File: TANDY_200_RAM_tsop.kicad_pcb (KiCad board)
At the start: 2 copper layers, 35.6 x 20.3 mm, 4 parts, among them J1 TANDY_26-3688, U1 62256, U2 74LVC2G00

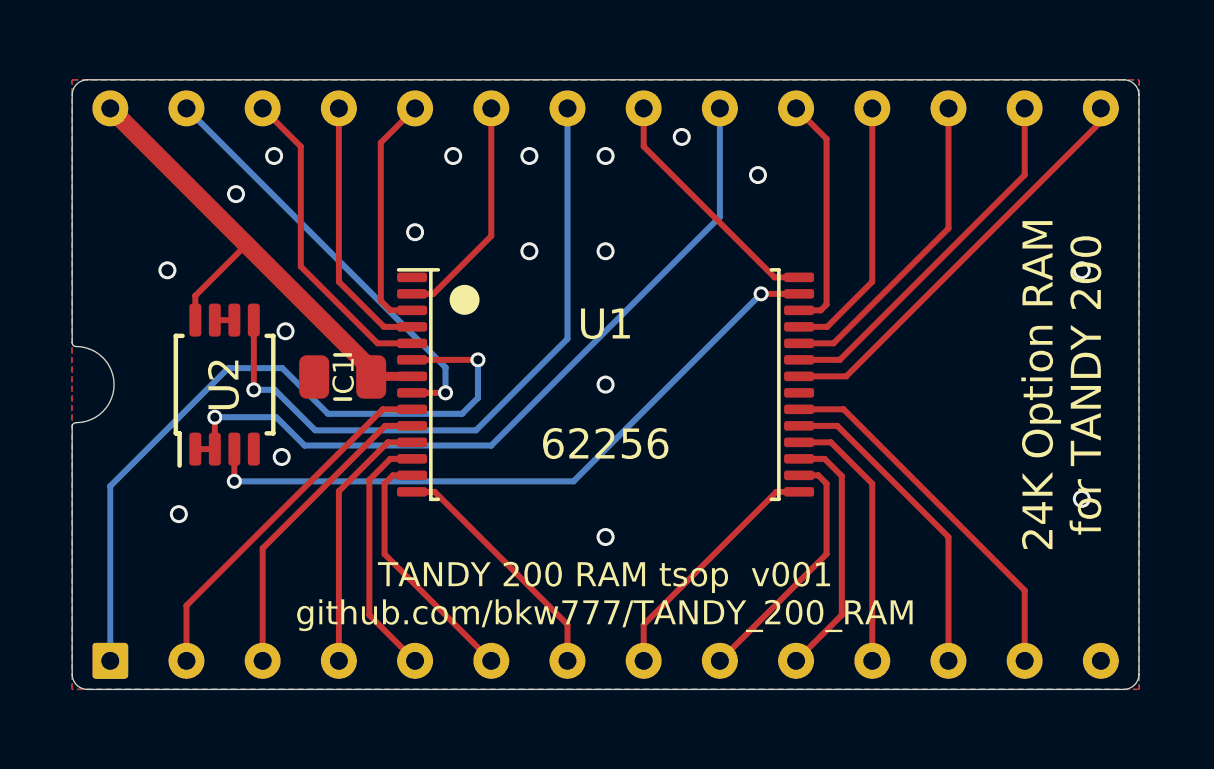
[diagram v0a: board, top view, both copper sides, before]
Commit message: ground paths, footprints, sch symbols
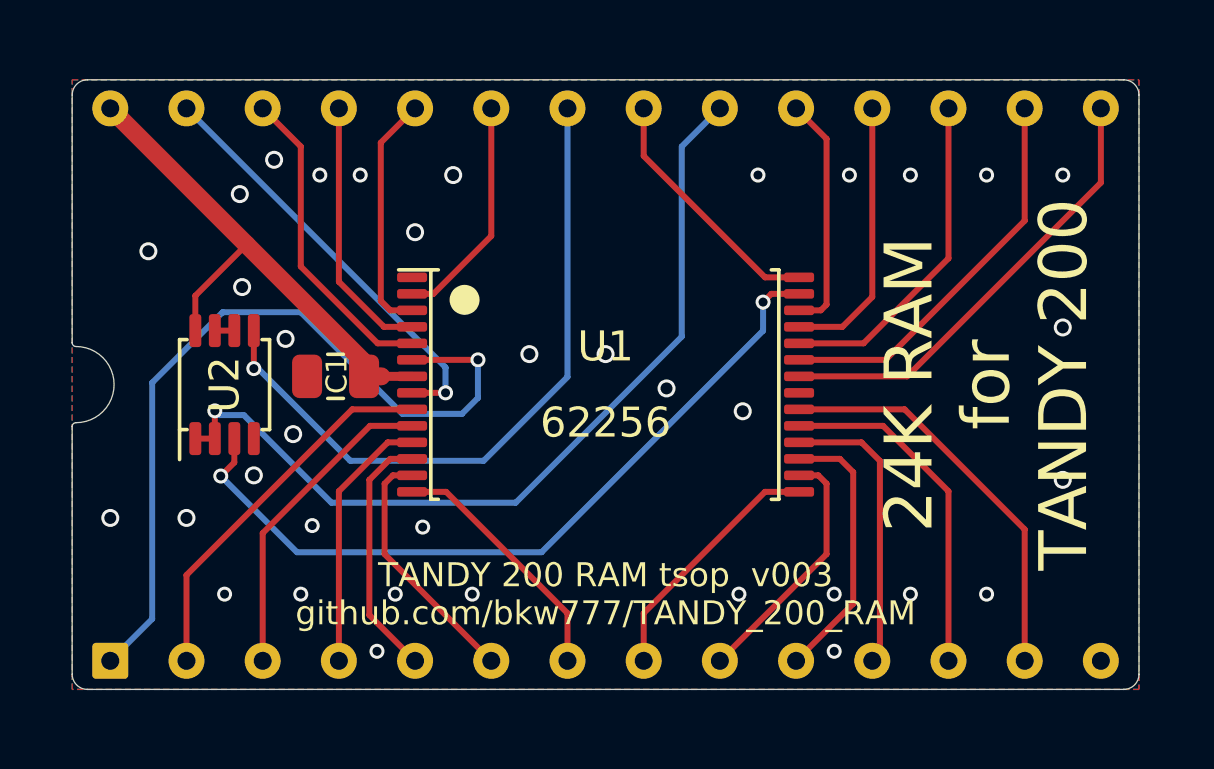
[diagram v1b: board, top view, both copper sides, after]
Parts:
- U1: footprint 000_LOCAL:TSOP-28-alt -> 000_LOCAL:TSOP-28
- U2: footprint 000_LOCAL:SOT-505-2 -> 000_LOCAL:SSOP-8_2.95x2.8x0.65
- moved C1 0.24 mm to (130.6, 105.6)
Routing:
- net /~{CE}: track 22.5 -> 25.9 mm
- net /~{CS1}: track 25.7 -> 28.8 mm
- net /~{WE}: track 24.0 -> 26.8 mm
- net /D2: track 12.4 -> 13.6 mm
- net /D3: track 14.0 -> 15.2 mm
- net /D1: track 10.6 -> 11.5 mm
- net /D4: track 12.3 -> 13.2 mm
- net /CS2: track 22.3 -> 23.1 mm
- net /D0: track 8.92 -> 9.72 mm
- net /A0: track 8.45 -> 9.07 mm
- net /A12: track 12.1 -> 12.7 mm
- net /D5: track 10.6 -> 11.2 mm
- net GND: vias 18 -> 36
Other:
- board text added: "24K RAM for TANDY 200"
- board text removed: "24K Option RAM for TANDY 200"

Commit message: 24k tsop layout and all board outlines expanded slightly
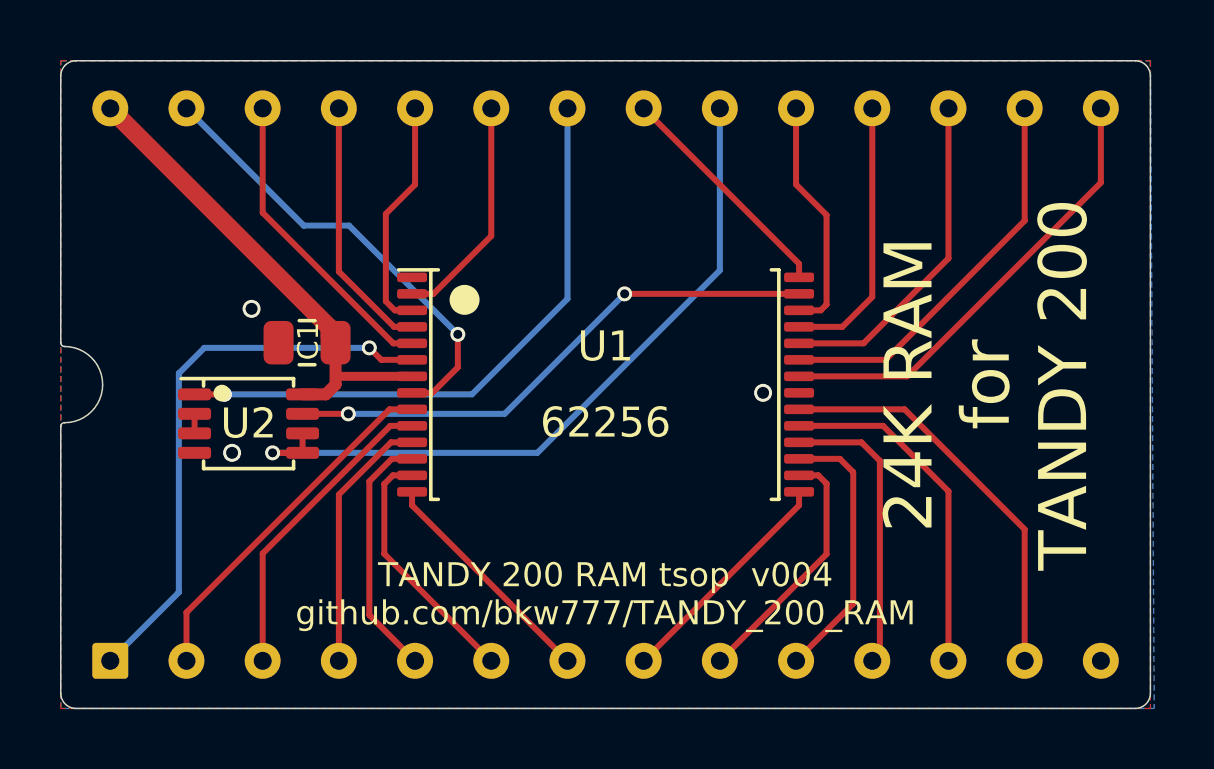
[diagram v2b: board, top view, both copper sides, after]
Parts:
- J1: footprint 000_LOCAL:KEL ICC05-028-360TP PCB -> 000_LOCAL:KEL ICC05-028-360TP
- moved U2 1.53 mm to (127.7, 107.2), turned to 0 degrees
- moved C1 1.47 mm to (129.6, 104.5)
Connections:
- U2 pad 1: /~{CS1} -> /CS2
- U2 pad 2: /~{CS1} -> Net-(U2-Pad2)
- U2 pad 3: /~{CE} -> Net-(U2-Pad2)
- U2 pad 5: /CS2 -> /~{CS1}
- U2 pad 6: Net-(U2-Pad6) -> /~{CS1}
- U2 pad 7: Net-(U2-Pad6) -> /~{CE}
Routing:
- net /~{WE}: track 26.8 -> 18.8 mm
- net /~{CE}: track 25.9 -> 18.2 mm
- net /~{CS1}: track 28.8 -> 24.5 mm
- net /CS2: track 23.1 -> 20.1 mm
- net VCC: track 17.6 -> 16.1 mm
- net /A14: track 14.2 -> 15.1 mm
- net /A12: track 12.7 -> 11.9 mm
- net /A3: track 8.44 -> 7.78 mm
- net /A2: track 8.44 -> 7.78 mm
- net /A10: track 8.44 -> 7.78 mm
- net Net-(U2-Pad6): track 0.65 -> 0.00 mm
- net Net-(U2-Pad2): track 0.00 -> 0.65 mm
- net GND: vias 36 -> 3
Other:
- board size 35.6 x 20.3 mm -> 36.3 x 21.6 mm
- board text added: "C1: ${f8b4e7cd-2ae3-4bf6-a8be-6993d42cff17:VALUE} U2: ${6711911d-c9dc-4aa5-b8c4-d291a8c627e2:VALUE} LEGS: Mill-Max 3121 or TE 1544210"
- board text removed: "C1: 0.1uF U2: 74LVC2G00 LEGS: Mill-Max 3121 or TE 1544210"
